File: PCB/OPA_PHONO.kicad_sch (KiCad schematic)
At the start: 6 parts, among them J1 PJRAS2X1S01X, J2 PJRAS2X1S01X, J3 UJC-HP-3-SMT-TR

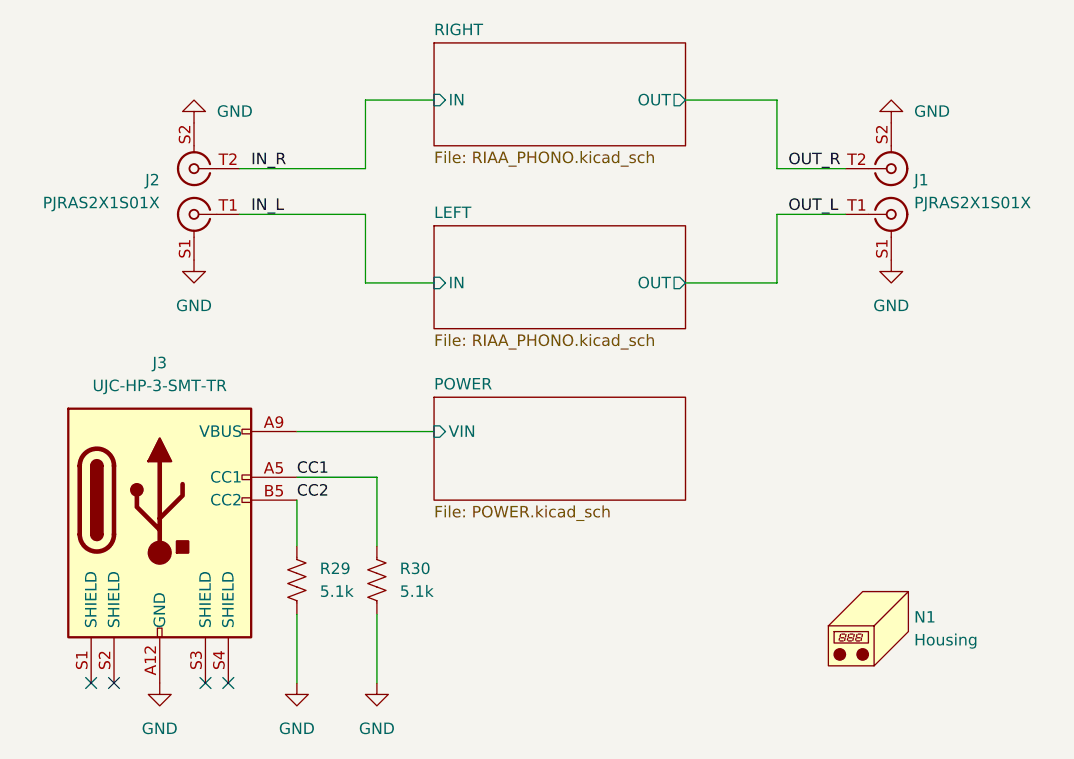
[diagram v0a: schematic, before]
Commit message: differential amp initial changes
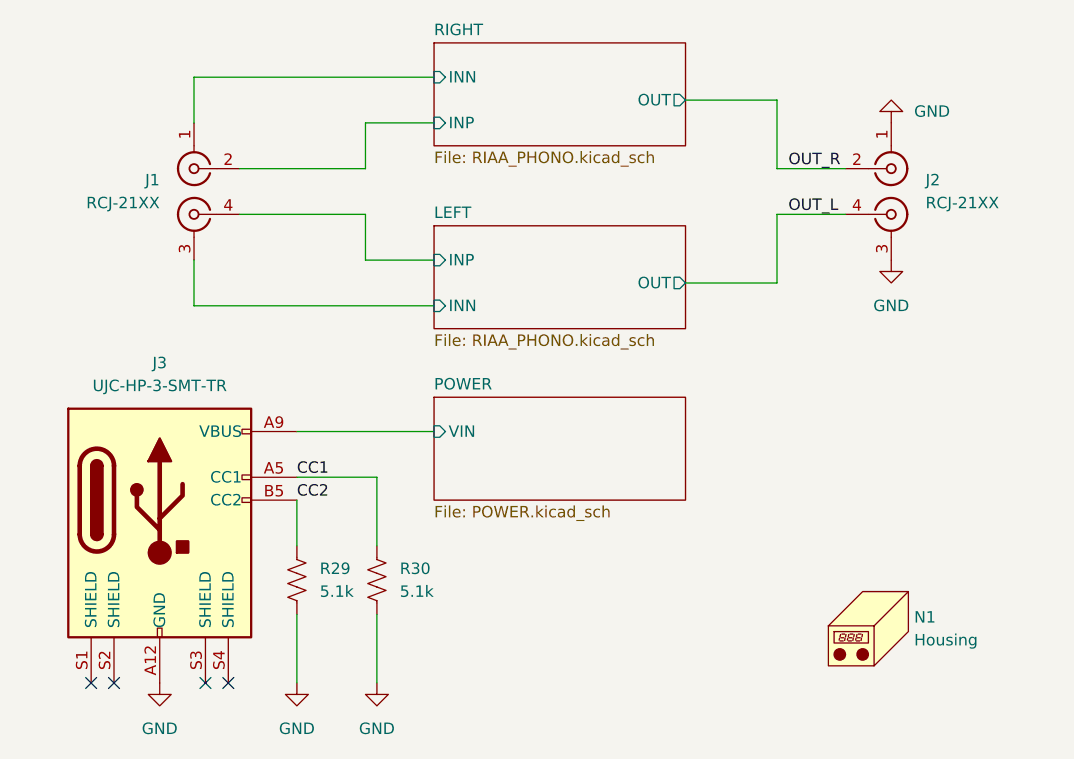
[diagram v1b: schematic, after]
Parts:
- removed J1, J2: PJRAS2X1S01X, OPA_PHONO:PJRAS2X1S01X, symbol OPA_PHONO:PJRAS2X1S01X
- added J1, J2: RCJ-21XX, LIB:RCJ-21XX, symbol OPA_PHONO:RCJ-21XX
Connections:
- net GND: now also J2.1 (Barrel_terminal_X1), J2.3 (Barrel_terminal_X2)
- net OUT_L: now also J2.4 (Center_terminal_X2)
- net OUT_R: now also J2.2 (Center_terminal_X1)
- new net LEFT/INN: J1.3 (Barrel_terminal_X2)
- new net LEFT/INP: J1.4 (Center_terminal_X2)
- new net RIGHT/INN: J1.1 (Barrel_terminal_X1)
- new net RIGHT/INP: J1.2 (Center_terminal_X1)
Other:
- sheet LEFT ports: added INN, INP; removed IN
- sheet RIGHT ports: added INN, INP; removed IN
